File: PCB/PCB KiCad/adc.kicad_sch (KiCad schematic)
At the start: 18 parts, among them U2 ADS1256IDBT, Y1 7.68MHz

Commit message: export for review
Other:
- company: (none) -> Plastic Scanner
- title: (none) -> Development Board
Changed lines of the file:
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@@
 (kicad_sch (version 20211123) (generator eeschema)
   (paper "A4")
+  (title_block
+    (title "Development Board")
+    (date "2022-03-15")
+    (rev "2.1")
+    (company "Plastic Scanner")
+  )
   (bus_alias "BUS1" (members "CLK" "MOSI" "MISO" "CS"))
   (junction (at 107.95 93.98) (diameter 0) (color 0 0 0 0)

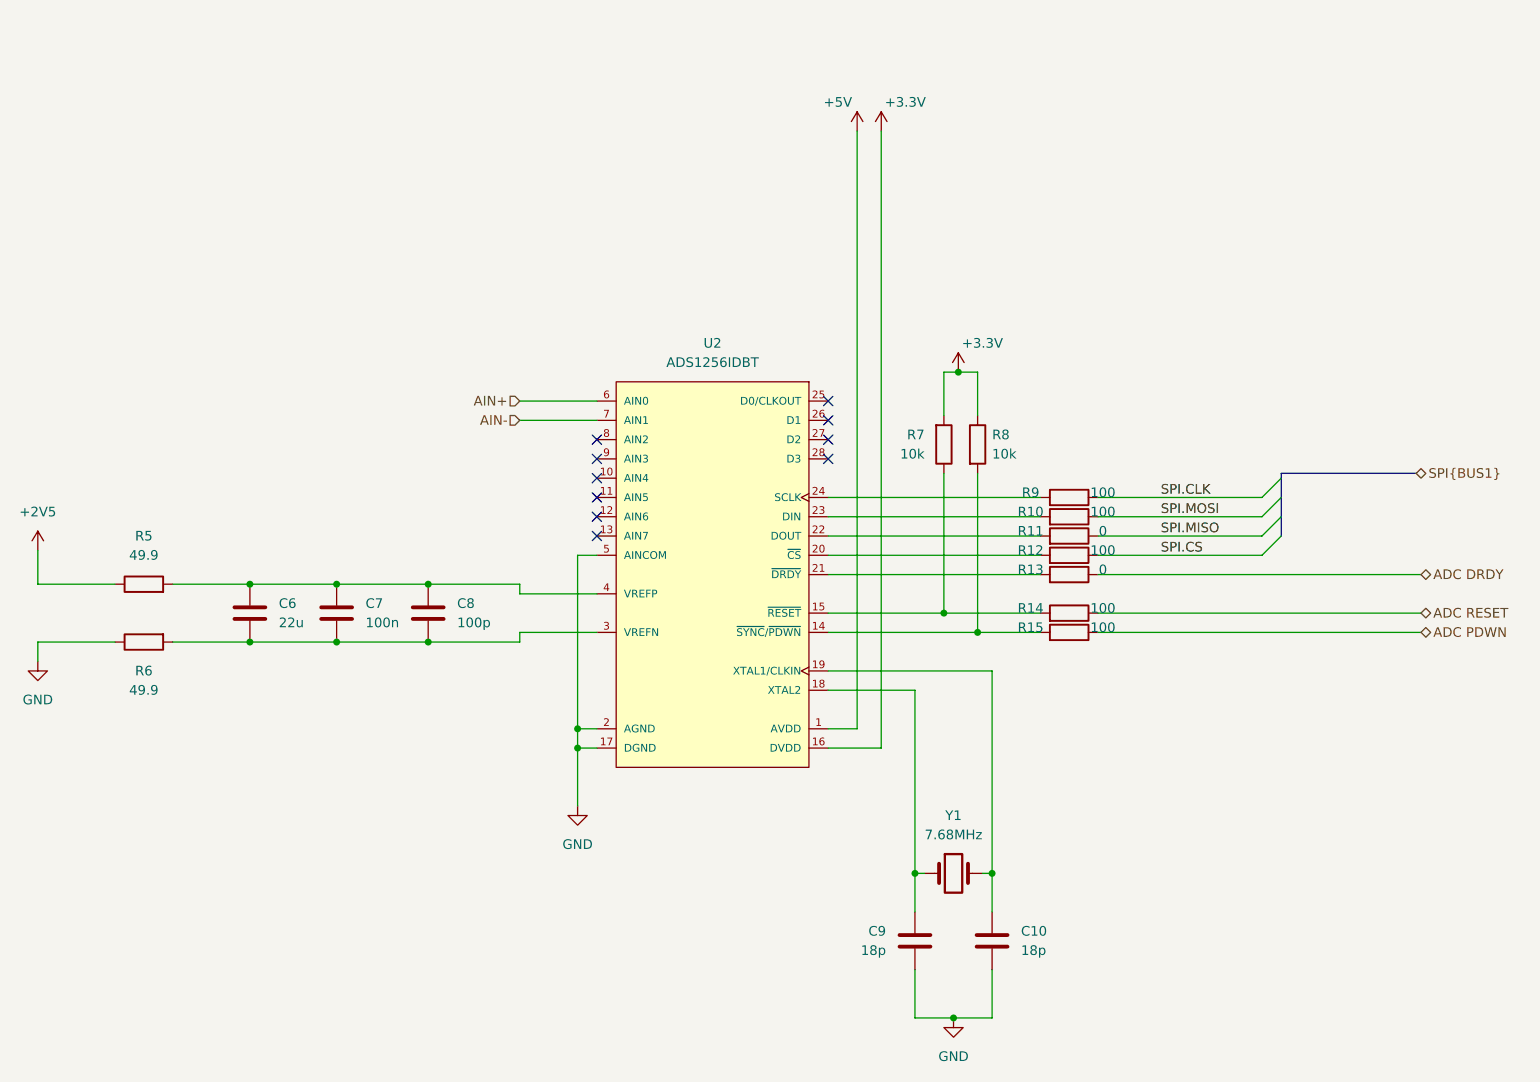
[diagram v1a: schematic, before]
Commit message: v2.2.0 first attempt for new ICs
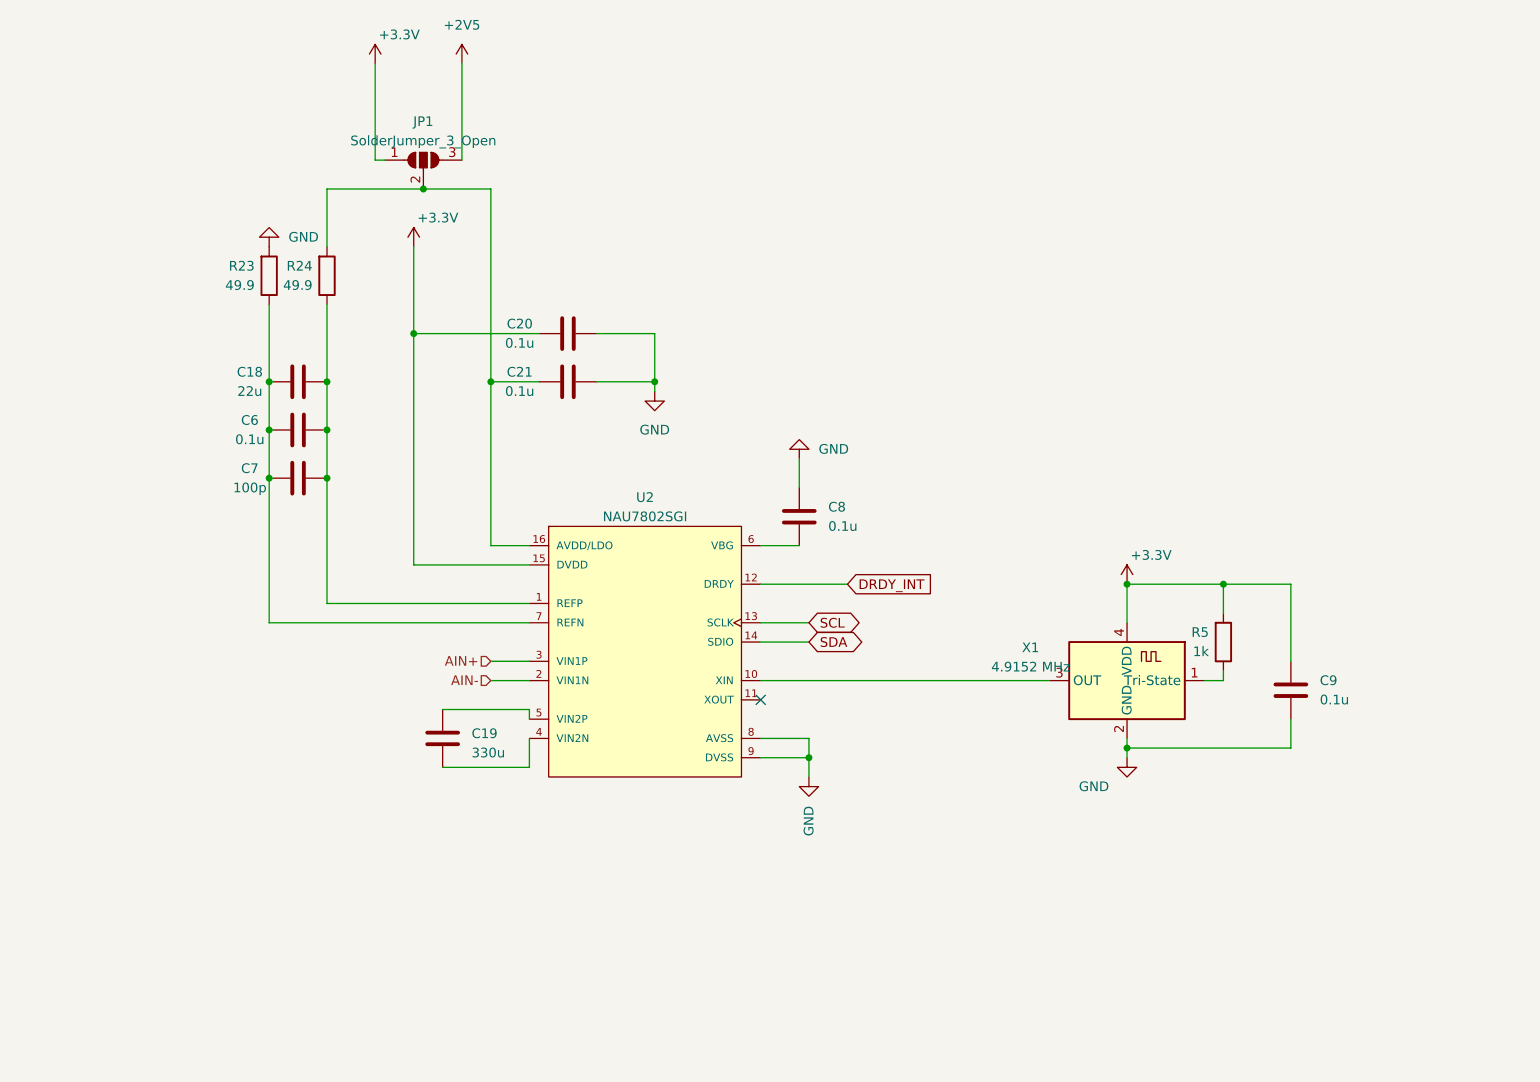
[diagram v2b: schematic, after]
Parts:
- removed C10: 18p, Capacitor_SMD:C_0805_2012Metric_Pad1.18x1.45mm_HandSolder, symbol Device:C
- removed R10, R12, R14, R15, R9: 100, Resistor_SMD:R_0805_2012Metric_Pad1.20x1.40mm_HandSolder, symbol Device:R
- removed R11, R13: 0, Resistor_SMD:R_0805_2012Metric_Pad1.20x1.40mm_HandSolder, symbol Device:R
- removed R6: 49.9, Resistor_SMD:R_0805_2012Metric_Pad1.20x1.40mm_HandSolder, symbol Device:R
- removed R7, R8: 10k, Resistor_SMD:R_0805_2012Metric_Pad1.20x1.40mm_HandSolder, symbol Device:R
- removed U2: ADS1256IDBT, ADS1256:Texas_Instruments-ADS1256IDBT-Level_A, symbol ADS1256:ADS1256IDBT
- removed Y1: 7.68MHz, Crystal:Crystal_HC49-U_Vertical, symbol Device:Crystal
- added C18: 22u, Capacitor_SMD:C_0805_2012Metric_Pad1.18x1.45mm_HandSolder, symbol Device:C
- added C19: 330u, Capacitor_SMD:C_0805_2012Metric_Pad1.18x1.45mm_HandSolder, symbol Device:C
- added C20, C21: 0.1u, Capacitor_SMD:C_0805_2012Metric_Pad1.18x1.45mm_HandSolder, symbol Device:C
- added JP1: SolderJumper_3_Open, Jumper:SolderJumper-3_P2.0mm_Open_TrianglePad1.0x1.5mm, symbol Jumper:SolderJumper_3_Open
- added R23, R24: 49.9, Resistor_SMD:R_0805_2012Metric_Pad1.20x1.40mm_HandSolder, symbol Device:R
- added U2: NAU7802SGI, IC_Nuvoton_NAU7802SGI:Nuvoton-NAU7802SGI-0-0-0, symbol NAU7802:NAU7802SGI
- added X1: 4.9152 MHz, Oscillator:Oscillator_SMD_ECS_2520MV-xxx-xx-4Pin_2.5x2.0mm, symbol Oscillator:ECS-2520MV-xxx-xx
- C6: value 22u -> 0.1u
- C7: value 100n -> 100p
- C8: value 100p -> 0.1u
- C9: value 18p -> 0.1u
- R5: value 49.9 -> 1k
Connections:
- net +2V5: now also JP1.3 (B); no longer R5.1
- net +3V3: now also C9.1, R5.2, C20.1, JP1.1 (A), U2.15 (DVDD), X1.4 (VDD)
- net AIN+: now also U2.3 (VIN1P)
- net AIN-: now also U2.2 (VIN1N)
- net GND: now also C8.1, C9.2, C20.2, C21.2, R23.2, U2.8 (AVSS), U2.9 (DVSS), X1.2 (GND); no longer C9.1
- net at C6.1, C7.1: now also C18.1, R23.1, U2.7 (REFN); no longer C8.1, R5.2
- net at C6.2, C7.2: now also C18.2, R24.1, U2.1 (REFP); no longer C8.2
- new net: C8.2, U2.6 (VBG)
- new net: U2.10 (XIN), X1.3 (OUT)
- new net: C21.1, JP1.2 (C), R24.2, U2.16 (AVDD/LDO)
- new net: C19.2, U2.4 (VIN2N)
- new net: C19.1, U2.5 (VIN2P)
- new net: R5.1, X1.1 (Tri-State)
- new net DRDY_INT: U2.12 (DRDY)
- new net SCL: U2.13 (SCLK)
- new net SDA: U2.14 (SDIO)
- no-connect marks 10 -> 1
